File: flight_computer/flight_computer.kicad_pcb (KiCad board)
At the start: 4 copper layers, 47 x 66 mm, 108 parts, among them J1 Conn_02x05_Odd_Even, J2 MEM2061-01-188-00-A_REVA, J3 Conn_01x02, J5 3817564, J7 Conn_01x07_MountingPin, Q1 Q_NPN_BEC, Q2 Q_NMOS_GSD, SW1 SW_Push, SW2 SW_Push, U1 STM8S007C8T6TR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

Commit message: DRC gone, not reviews yet
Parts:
- C33, C34, C35, C36, R24, R25, U8: moved to B.Cu
- moved C33 20.4 mm to (142.3, 82.4)
- moved R24 16.2 mm to (140.5, 79.2)
- moved C35 15.3 mm to (140.0, 80.7), turned to 180 degrees
- moved C34 13.5 mm to (139.1, 79.7), turned to 180 degrees
- moved U8 13.3 mm to (139.0, 84.9)
- moved C36 11.9 mm to (138.2, 80.7), turned to 180 degrees
- moved R25 11.0 mm to (137.7, 79.2)
- moved C5 0.10 mm to (134.6, 113.3)
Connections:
- U9 pad 5: (no net) -> GND
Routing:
- net /SPI_SCK: track 47.0 -> 57.2 mm, vias 2 -> 5
- net /Temperature sensor/T+: track 18.9 -> 8.85 mm
- net /SPI_MISO: track 42.0 -> 50.4 mm, vias 1 -> 2
- net GND: track 103.5 -> 110.0 mm, vias 77 -> 131
- net /TC_CS: track 35.6 -> 40.6 mm
- net /Microcontroller/3V3D: track 50.5 -> 48.9 mm
- net /Microcontroller/VBATT_{SENSE}: track 33.8 -> 34.7 mm

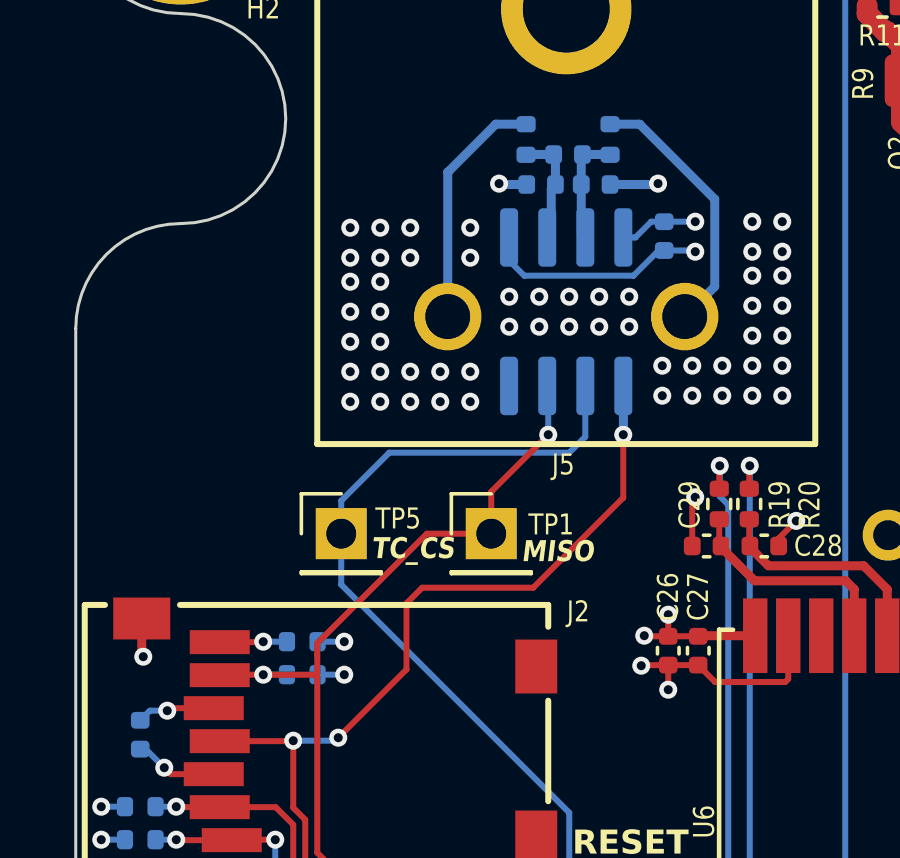
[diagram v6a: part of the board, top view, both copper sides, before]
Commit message: Most warnings gone now too
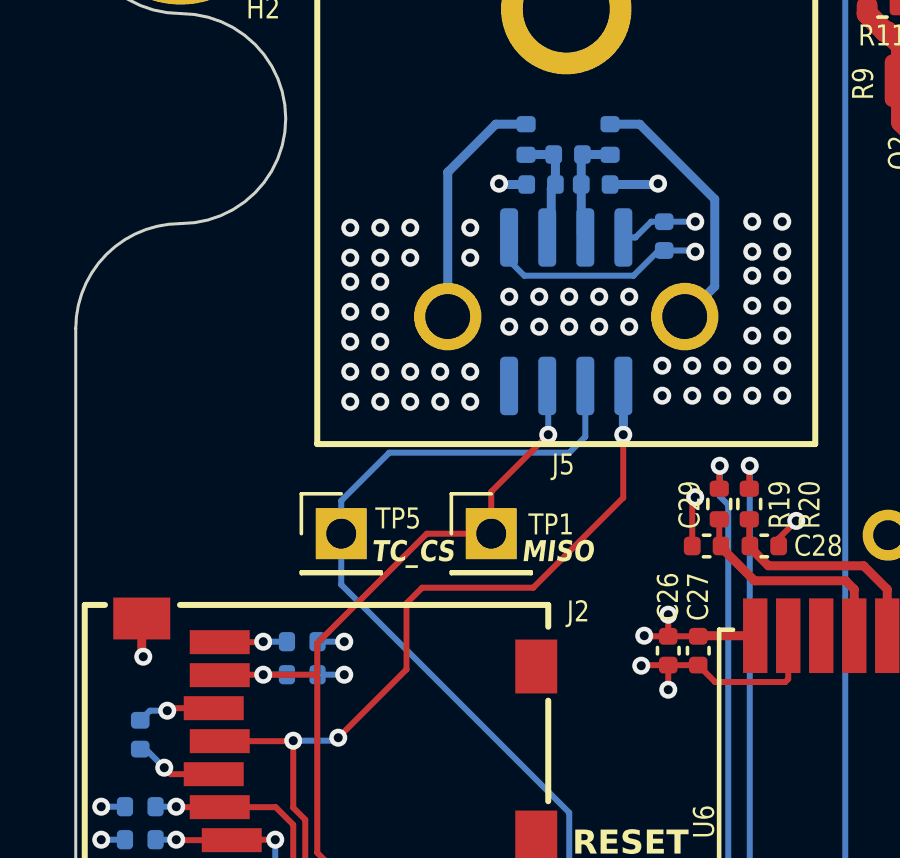
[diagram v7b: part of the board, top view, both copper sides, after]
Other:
- board text removed: "0.1521 controlled impedance trace width For JLC04161H-3313 4 layer stackup Ref plane L2, siglan L1 1oz outer, 0.5oz inner coplanar waveguide with 0.25mm to waveguide"
- board text removed: "0.6431 mm controlled impedance trace width For JLC04161H-7628B 4 layer stackup Signal L1, ref plane L2 1oz outer, 0.0152mm inner coplanar waveguide with 0.22mm to waveguide"
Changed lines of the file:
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@@
     (effects (font (size 0.7 0.6) (thickness 0.15) bold) (justify left bottom))
   )
-  (gr_text "TC_CS" (at 132.5 93.2) (layer "F.SilkS")
+  (gr_text "TC_CS" (at 132.5 93.3) (layer "F.SilkS")
     (effects (font (size 0.7 0.6) (thickness 0.15) bold italic) (justify left bottom))
   )
@@
     (effects (font (size 0.7 0.6) (thickness 0.15) bold) (justify left bottom))
   )
-  (gr_text "0.1521 controlled impedance trace width\nFor JLC04161H-3313 4 layer stackup\nRef plane L2, siglan L1\n1oz outer, 0.5oz inner\ncoplanar waveguide with 0.25mm to waveguide" (at 179.95 85.42) (layer "Cmts.User")
-    (effects (font (size 1 1) (thickness 0.15)) (justify left bottom))
-  )
   (gr_text "0.3421 mm controlled impedance trace width\nFor JLC04161H-7628 4 layer stackup 1.6mm\nSignal L1, ref plane L2\n1oz outer, 0.0152mm inner\ncoplanar waveguide with 0.5mm to waveguide pour" (at 179.84 104.65) (layer "Cmts.User")
-    (effects (font (size 1 1) (thickness 0.15)) (justify left bottom))
-  )
-  (gr_text "0.6431 mm controlled impedance trace width\nFor JLC04161H-7628B 4 layer stackup\nSignal L1, ref plane L2\n1oz outer, 0.0152mm inner\ncoplanar waveguide with 0.22mm to waveguide" (at 180 94.7) (layer "Cmts.User")
     (effects (font (size 1 1) (thickness 0.15)) (justify left bottom))
   )
@@
   (segment (start 139.5 79.7) (end 139.54 79.66) (width 0.3) (layer "B.Cu") (net 21))
   (segment (start 139.5 80.66) (end 139.5 82.29) (width 0.3) (layer "B.Cu") (net 21))
-  (segment (start 139.43 80.73) (end 139.5 80.66) (width 0.3) (layer "B.Cu") (net 21))
   (segment (start 140.45 79.66) (end 140.46 79.67) (width 0.3) (layer "B.Cu") (net 21))
   (segment (start 139.54 79.66) (end 140.45 79.66) (width 0.3) (layer "B.Cu") (net 21))
@@
   (segment (start 127.465 97) (end 127.45 97.015) (width 0.2) (layer "F.Cu") (net 38))
   (segment (start 148.1 111.7) (end 147.6 111.2) (width 0.2) (layer "F.Cu") (net 38))
-  (segment (start 130.7 96.341396) (end 130.7 95.951471) (width 0.2) (layer "F.Cu") (net 38))
+  (segment (start 130.7 97) (end 130.7 95.951471) (width 0.2) (layer "F.Cu") (net 38))
   (segment (start 148.1 113.955329) (end 148.1 111.7) (width 0.2) (layer "F.Cu") (net 38))
   (segment (start 148.7625 115.85) (end 147.872335 115.85) (width 0.2) (layer "F.Cu") (net 38))
@@
   (segment (start 130.7 95.951471) (end 134.351471 92.3) (width 0.2) (layer "F.Cu") (net 38))
   (segment (start 147.725 115.702665) (end 147.725 114.330329) (width 0.2) (layer "F.Cu") (net 38))
-  (segment (start 130.7 97) (end 130.7 96.341396) (width 0.2) (layer "F.Cu") (net 38))
   (segment (start 137.365686 109.6) (end 130.7 102.934314) (width 0.2) (layer "F.Cu") (net 38))
   (segment (start 147.725 114.330329) (end 148.1 113.955329) (width 0.2) (layer "F.Cu") (net 38))

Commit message: PCB review done
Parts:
- added G***: LOGO, my_footprints:Nuke_logo7x7.8mm, F.Cu at (126.6, 88.8)
- added G***: LOGO, LOGO, B.Cu at (154.9, 82.5)
